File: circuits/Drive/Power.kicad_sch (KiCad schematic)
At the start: 81 parts, among them IC1 DCDC_MPM3620A, J10 Conn_01x02_Male, J11 Conn_01x02_Male, J12 Conn_01x02_Male, J13 Conn_01x02_Male, J6 USB_C_Receptacle_USB2.0, J9 Conn_01x02_Male, Q16 SSM6J808R, Q17 SSM6J808R, Q18 SSM3J332R, Q19 S8550, Q2 BSS138, Q20 SSM3J332R, Q21 S8550, Q23 S8550, Q24 SSM3J332R, Q25 S8550, Q3 SSM3J332R, Q4 BSS138, SW1 SW_SPDT_White

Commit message: ラズパイ基板とか
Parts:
- R19, R20, R65: value 2k -> 1k
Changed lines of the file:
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@@
       (effects (font (size 1.27 1.27)))
     )
-    (property "Value" "2k" (at 335.28 210.82 90)
+    (property "Value" "1k" (at 335.28 210.82 90)
       (effects (font (size 1.27 1.27)))
     )
@@
       (effects (font (size 1.27 1.27)))
     )
-    (property "Value" "2k" (at 335.28 198.12 90)
+    (property "Value" "1k" (at 335.28 198.12 90)
       (effects (font (size 1.27 1.27)))
     )
@@
       (effects (font (size 1.27 1.27)))
     )
-    (property "Value" "2k" (at 335.28 223.52 90)
+    (property "Value" "1k" (at 335.28 223.52 90)
       (effects (font (size 1.27 1.27)))
     )

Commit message: PDFプロット
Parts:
- added U1: AZ1084CD-3.3, Package_TO_SOT_SMD:TO-252-2, symbol Regulator_Linear:AMS1117CD-3.3
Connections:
- net +3.3V: now also U1.2 (VO)
- net +5V: now also U1.3 (VI)
- net GND: now also U1.1 (GND)
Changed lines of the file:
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@@
+    )
+  )
+  (symbol (lib_id "Regulator_Linear:AMS1117CD-3.3") (at 236.22 213.36 0) (unit 1)
+    (in_bom yes) (on_board yes) (dnp no) (fields_autoplaced)
+    (property "Reference" "U1" (at 236.22 207.01 0)
+      (effects (font (size 1.27 1.27)))
+    )
+    (property "Value" "AZ1084CD-3.3" (at 236.22 209.55 0)
+      (effects (font (size 1.27 1.27)))
+    )
+    (property "Footprint" "Package_TO_SOT_SMD:TO-252-2" (at 236.22 208.28 0)
+      (effects (font (size 1.27 1.27)) hide)
+    )
+    (property "Datasheet" "http://www.advanced-monolithic.com/pdf/ds1117.pdf" (at 238.76 219.71 0)
+      (effects (font (size 1.27 1.27)) hide)
+    )
+    (pin "1")
+    (pin "2")
+    (pin "3")
+    (instances
+      (project "Drive"
+        (path "/bf4fa0f7-7e40-4646-9c11-e04533c904d6/78bba271-6f80-468f-a85b-9d4b16f8bee8"
+          (reference "U1") (unit 1)
+        )
+      )
     )
   )

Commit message: panelフットプリント配置
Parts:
- U1: value AZ1084CD-3.3 -> AZ1117CH-3.3; footprint Package_TO_SOT_SMD:TO-252-2 -> Package_TO_SOT_SMD:SOT-223-3_TabPin2
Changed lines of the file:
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@@
-    )
-  )
-  (symbol (lib_id "Regulator_Linear:AMS1117CD-3.3") (at 236.22 213.36 0) (unit 1)
-    (in_bom yes) (on_board yes) (dnp no) (fields_autoplaced)
-    (property "Reference" "U1" (at 236.22 207.01 0)
-      (effects (font (size 1.27 1.27)))
-    )
-    (property "Value" "AZ1084CD-3.3" (at 236.22 209.55 0)
-      (effects (font (size 1.27 1.27)))
-    )
-    (property "Footprint" "Package_TO_SOT_SMD:TO-252-2" (at 236.22 208.28 0)
-      (effects (font (size 1.27 1.27)) hide)
-    )
-    (property "Datasheet" "http://www.advanced-monolithic.com/pdf/ds1117.pdf" (at 238.76 219.71 0)
-      (effects (font (size 1.27 1.27)) hide)
-    )
-    (pin "1")
-    (pin "2")
-    (pin "3")
-    (instances
-      (project "Drive"
-        (path "/bf4fa0f7-7e40-4646-9c11-e04533c904d6/78bba271-6f80-468f-a85b-9d4b16f8bee8"
-          (reference "U1") (unit 1)
-        )
-      )
     )
   )
@@
         )
       )
+    )
+  )
+  (symbol (lib_id "Regulator_Linear:AMS1117CD-3.3") (at 236.22 213.36 0) (unit 1)
+    (in_bom yes) (on_board yes) (dnp no) (fields_autoplaced)
+    (property "Reference" "U1" (at 236.22 207.01 0)
+      (effects (font (size 1.27 1.27)))
+    )
+    (property "Value" "AZ1117CH-3.3" (at 236.22 209.55 0)
+      (effects (font (size 1.27 1.27)))
+    )
+    (property "Footprint" "Package_TO_SOT_SMD:SOT-223-3_TabPin2" (at 236.22 208.28 0)
+      (effects (font (size 1.27 1.27)) hide)
+    )
+    (property "Datasheet" "http://www.advanced-monolithic.com/pdf/ds1117.pdf" (at 238.76 219.71 0)
+      (effects (font (size 1.27 1.27)) hide)
+    )
+    (pin "1")
+    (pin "2")
+    (pin "3")
+    (instances
+      (project "Drive"
+        (path "/bf4fa0f7-7e40-4646-9c11-e04533c904d6/78bba271-6f80-468f-a85b-9d4b16f8bee8"
+          (reference "U1") (unit 1)
+        )
+      )

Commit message: シンボル・フットプリントMyLib->TomoshibiLib置き換え
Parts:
- IC1: footprint MyLibrary:DCDC_MPM3620A -> TomoshibiLibrary:DCDC_MPM3620A; symbol MyLibrary:DCDC_MPM3620A -> TomoshibiLibrary:DCDC_MPM3620A
- L1: footprint MyLibrary:Inductor_CDPH4D19F -> TomoshibiLibrary:Inductor_CDPH4D19F
- Q16, Q17: footprint MyLibrary:Package_TSOP6F -> TomoshibiLibrary:Package_TSOP6F
- SW1: footprint MyLibrary:SW_Slide_SPDT_White -> TomoshibiLibrary:SW_Slide_SPDT_White
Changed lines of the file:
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@@
       (effects (font (size 1.27 1.27)))
     )
-    (property "Footprint" "MyLibrary:Inductor_CDPH4D19F" (at 246.38 71.12 0)
+    (property "Footprint" "TomoshibiLibrary:Inductor_CDPH4D19F" (at 246.38 71.12 0)
       (effects (font (size 1.27 1.27)) hide)
     )
@@
     )
   )
-  (symbol (lib_id "MyLibrary:DCDC_MPM3620A") (at 119.38 137.16 0) (unit 1)
+  (symbol (lib_id "TomoshibiLibrary:DCDC_MPM3620A") (at 119.38 137.16 0) (unit 1)
     (in_bom yes) (on_board yes) (dnp no)
     (property "Reference" "IC1" (at 134.62 133.35 0)
@@
       (effects (font (size 1.27 1.27)))
     )
-    (property "Footprint" "MyLibrary:DCDC_MPM3620A" (at 148.59 232.08 0)
+    (property "Footprint" "TomoshibiLibrary:DCDC_MPM3620A" (at 104.14 100.66 0)
       (effects (font (size 1.27 1.27)) (justify left top) hide)
     )
-    (property "Datasheet" "http://www.monolithicpower.com/DesktopModules/DocumentManage/API/Document/getDocument?id=3961" (at 148.59 332.08 0)
+    (property "Datasheet" "http://www.monolithicpower.com/DesktopModules/DocumentManage/API/Document/getDocument?id=3961" (at 104.14 200.66 0)
       (effects (font (size 1.27 1.27)) (justify left top) hide)
     )
@@
       (effects (font (size 1.27 1.27)))
     )
-    (property "Footprint" "MyLibrary:SW_Slide_SPDT_White" (at 203.2 40.64 0)
+    (property "Footprint" "TomoshibiLibrary:SW_Slide_SPDT_White" (at 203.2 40.64 0)
       (effects (font (size 1.27 1.27)) hide)
     )
@@
       (effects (font (size 1.27 1.27)))
     )
-    (property "Footprint" "MyLibrary:Package_TSOP6F" (at 213.36 68.58 0)
+    (property "Footprint" "TomoshibiLibrary:Package_TSOP6F" (at 213.36 68.58 0)
       (effects (font (size 1.27 1.27)) (justify left) hide)
     )
@@
       (effects (font (size 1.27 1.27)))
     )
-    (property "Footprint" "MyLibrary:Package_TSOP6F" (at 187.96 68.58 0)
+    (property "Footprint" "TomoshibiLibrary:Package_TSOP6F" (at 187.96 68.58 0)
       (effects (font (size 1.27 1.27)) (justify left) hide)
     )

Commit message: 更新
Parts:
- removed C25, C26, C39: 470uF, symbol Device:C_Polarized
- removed IC1: DCDC_MPM3620A, TomoshibiLibrary:DCDC_MPM3620A, symbol TomoshibiLibrary:DCDC_MPM3620A
- removed J10, J11, J12, J13, J9: Conn_01x02_Male, Connector_Molex:Molex_SPOX_5267-02A_1x02_P2.50mm_Vertical, symbol Connector:Conn_01x02_Male
- removed J6: USB_C_Receptacle_USB2.0, Connector_USB:USB_C_Receptacle_G-Switch_GT-USB-7010ASV, symbol Connector:USB_C_Receptacle_USB2.0
- removed Q2, Q4: BSS138, Package_TO_SOT_SMD:SOT-23, symbol Device:Q_NMOS_GSD
- removed R3: 200k, Resistor_SMD:R_0402_1005Metric, symbol Device:R
- added C11: 1uF, Capacitor_SMD:C_0402_1005Metric, symbol Device:C
- added C25, C26, C41: 22uF, Capacitor_SMD:C_0805_2012Metric, symbol Device:C
- added H1, H2: MountingHole_Pad, MountingHole:MountingHole_3.2mm_M3_Pad_Via, symbol Mechanical:MountingHole_Pad
- added J11, J2, J3, J4, J5: Conn_01x02_Pin, Connector_Molex:Molex_SPOX_5268-02A_1x02_P2.50mm_Horizontal, symbol Connector:Conn_01x02_Pin
- added J7: USB_C_Receptacle_PowerOnly_6P, Connector_USB:USB_C_Receptacle_GCT_USB4125-xx-x_6P_TopMnt_Horizontal, symbol Connector:USB_C_Receptacle_PowerOnly_6P
- added Q5, Q8: 2N7002, Package_TO_SOT_SMD:SOT-23, symbol Transistor_FET:2N7002
- added U2: DCDC_TPSM336x5, TomoshibiLibrary:DCDC_TPSM336x5, symbol TomoshibiLibrary:DCDC_TPSM336x5
- C23, C37, C38, C6: value 470uF -> 47uF; footprint (none) -> Capacitor_SMD:CP_Elec_6.3x5.4
- C32, C33: value 470uF -> 100uF; footprint (none) -> TomoshibiLibrary:Capacitor_Alum_Radial_5.0x11.0mm_Horizontal
- L1: value 22uH -> 1uH; footprint TomoshibiLibrary:Inductor_CDPH4D19F -> Inductor_SMD:L_0603_1608Metric
- R4: value 100k -> 10k
- R5: value 12k -> 20k
- R6: value 2.2k -> 5.1k
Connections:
- net +3.3V: now also C26.1
- net +5V: now also C25.1
- net +BATT: now also H1.1, J11.2 (Pin_2), J2.2 (Pin_2), J3.2 (Pin_2), J4.2 (Pin_2), J5.2 (Pin_2); no longer C38.1
- net GND: now also C11.2, C25.2, C26.2, C41.2, H2.1, J11.1 (Pin_1), J2.1 (Pin_1), J3.1 (Pin_1), J4.1 (Pin_1), J5.1 (Pin_1), J7.A12 (GND), J7.B12 (GND), J7.S1 (SHIELD), Q5.2 (S), Q8.2 (S), U2.10 (GND)
- net PG: now also R4.2, Q5.1 (G), U2.1 (PGOOD); no longer R4.1
- net PowerSW: now also Q8.1 (G)
- net VBUS: now also J7.A9 (VBUS), J7.B9 (VBUS)
- net VCC: now also C38.1, U2.2 (EN), U2.3 (VIN)
- net Vout: now also C41.1, U2.4 (VOUT)
- net at Q3.1 (G), R8.2: now also Q5.3 (D)
- net at R5.1, R6.2: now also U2.9 (FB)
- net at R64.2: now also J7.B5 (CC2)
- net at R12.2: now also Q8.3 (D)
- net at R65.2: now also J7.A5 (CC1)
- net at R1.1: now also SW1.3 (C); no longer SW1.1 (A)
- new net: C11.1, R4.1, U2.11 (RT), U2.8 (VCC)
- no-connect marks 11 -> 4
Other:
- note removed: "三端子を新しく選定したのにする 電源直付けのための穴を設定する 電源平滑コンデンサは基板設計の時に良い感じに数調整"
- note removed: "電源スイッチ 耐圧大丈夫？"
- moved on the sheet: C1, C2, C38, C40, C6, D1, Q3, R10, R4, R5, R6, R64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

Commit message: raspi基板回路図
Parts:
- SW1: footprint TomoshibiLibrary:SW_Slide_SPDT_White -> TomoshibiLibrary:SW_Slide_SPDT_IS-1235-G
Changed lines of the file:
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@@
       (effects (font (size 1.27 1.27)))
     )
-    (property "Footprint" "TomoshibiLibrary:SW_Slide_SPDT_White" (at 203.2 40.64 0)
+    (property "Footprint" "TomoshibiLibrary:SW_Slide_SPDT_IS-1235-G" (at 203.2 40.64 0)
       (effects (font (size 1.27 1.27)) hide)
     )

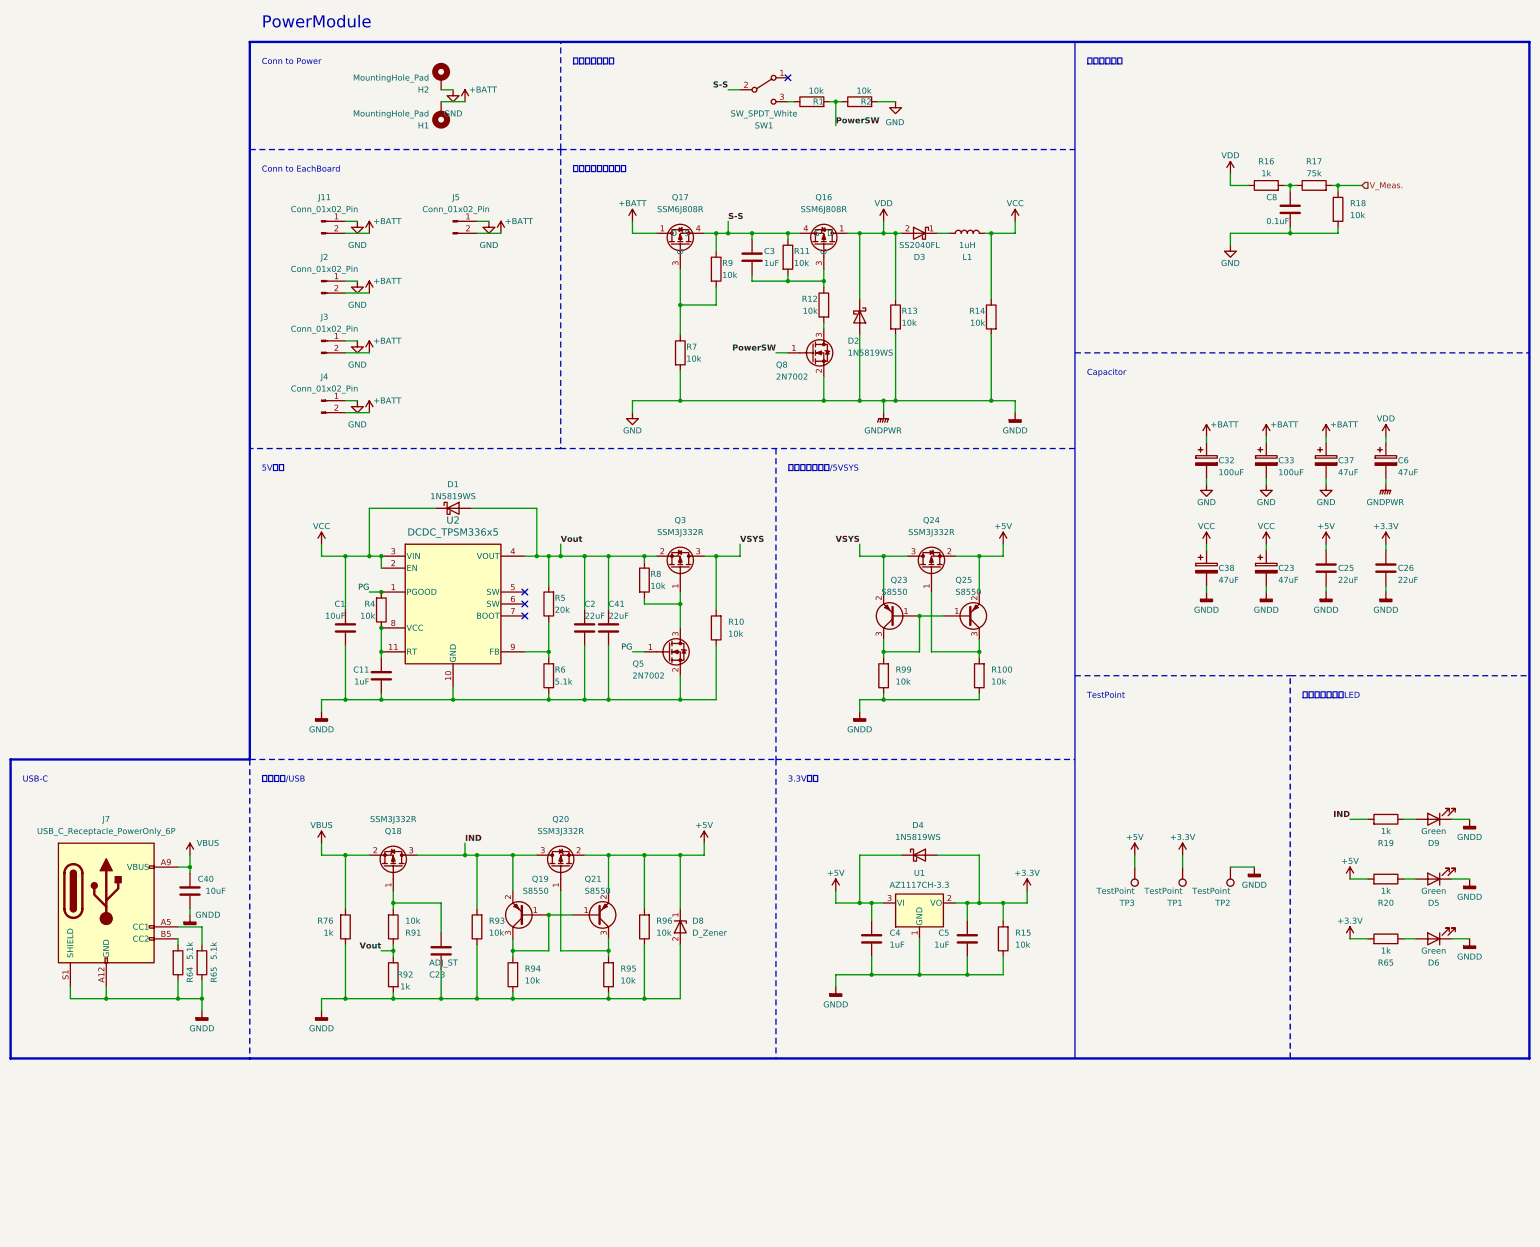
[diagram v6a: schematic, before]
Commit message: 発注_第一弾
Drive, 1stLayer_Power, 2ndLayer_3rdLayer
を発注
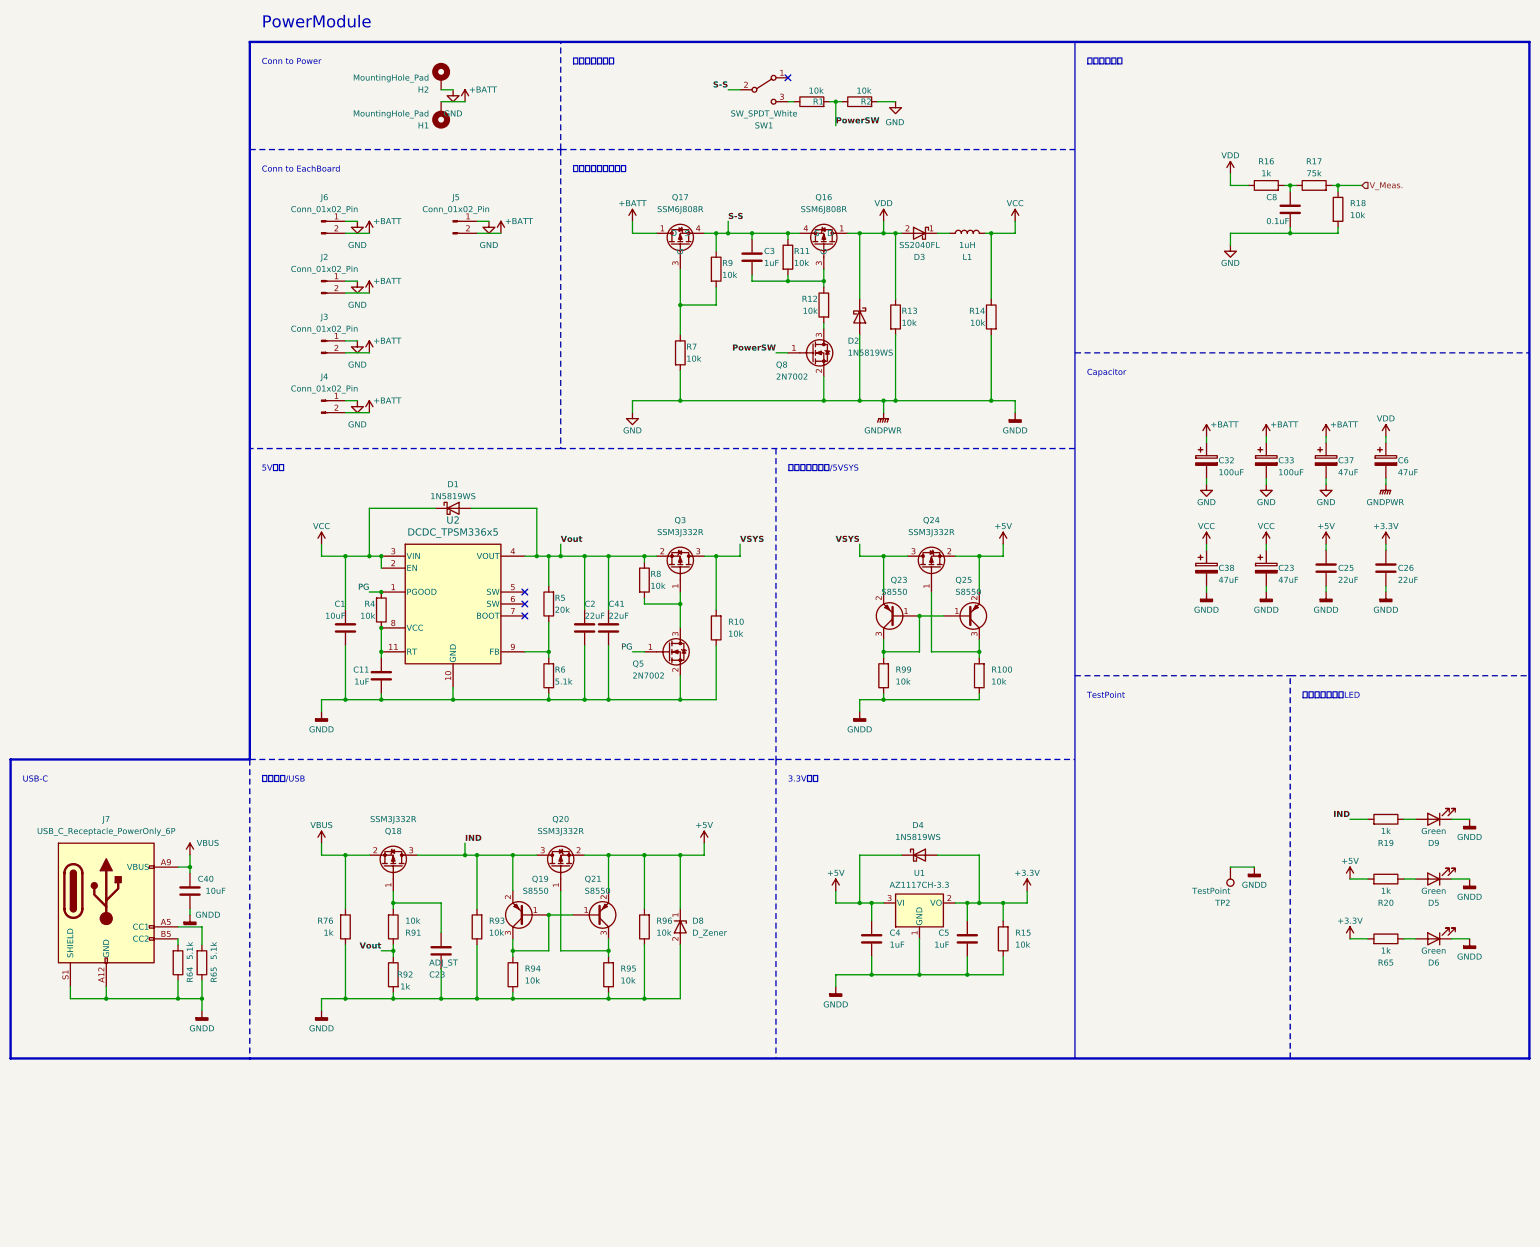
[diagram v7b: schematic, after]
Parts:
- removed TP1, TP3: TestPoint, TestPoint:TestPoint_THTPad_D2.0mm_Drill1.0mm, symbol Connector:TestPoint
- renumbered J11 to J6
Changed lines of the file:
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@@
     (stroke (width 0) (type default))
   )
-  (wire (pts (xy 292.1 203.2) (xy 292.1 205.74))
-    (stroke (width 0) (type default))
-  )
   (polyline (pts (xy 93.98 30.48) (xy 365.76 30.48))
     (stroke (width 0.5) (type solid))
@@
     (stroke (width 0) (type default))
   )
-  (wire (pts (xy 281.94 203.2) (xy 281.94 205.74))
-    (stroke (width 0) (type default))
-  )
   (wire (pts (xy 109.22 170.18) (xy 109.22 172.72))
     (stroke (width 0) (type default))
@@
     )
   )
-  (symbol (lib_id "Connector:TestPoint") (at 292.1 205.74 180) (unit 1)
-    (in_bom yes) (on_board yes) (dnp no)
-    (property "Reference" "TP1" (at 292.1 213.36 0)
-      (effects (font (size 1.27 1.27)) (justify left))
-    )
-    (property "Value" "TestPoint" (at 292.1 210.82 0)
-      (effects (font (size 1.27 1.27)) (justify left))
-    )
-    (property "Footprint" "TestPoint:TestPoint_THTPad_D2.0mm_Drill1.0mm" (at 287.02 205.74 0)
-      (effects (font (size 1.27 1.27)) hide)
-    )
-    (property "Datasheet" "~" (at 287.02 205.74 0)
-      (effects (font (size 1.27 1.27)) hide)
-    )
-    (pin "1")
-    (instances
-      (project "Main"
-        (path "/aa9d7141-7530-418f-853d-a56ee68433fb/a9430107-cf2a-4437-9d5a-ed3d69145a18"
-          (reference "TP1") (unit 1)
-        )
-      )
-      (project "Drive"
-        (path "/bf4fa0f7-7e40-4646-9c11-e04533c904d6/78bba271-6f80-468f-a85b-9d4b16f8bee8"
-          (reference "TP2") (unit 1)
-        )
-      )
-    )
-  )
   (symbol (lib_id "Device:C") (at 121.92 165.1 0) (mirror y) (unit 1)
     (in_bom yes) (on_board yes) (dnp no)
@@
     )
   )
-  (symbol (lib_id "power:+5V") (at 281.94 203.2 0) (unit 1)
-    (in_bom yes) (on_board yes) (dnp no) (fields_autoplaced)
-    (property "Reference" "#PWR06" (at 281.94 207.01 0)
-      (effects (font (size 1.27 1.27)) hide)
-    )
-    (property "Value" "+5V" (at 281.94 199.39 0)
-      (effects (font (size 1.27 1.27)))
-    )
-    (property "Footprint" "" (at 281.94 203.2 0)
-      (effects (font (size 1.27 1.27)) hide)
-    )
-    (property "Datasheet" "" (at 281.94 203.2 0)
-      (effects (font (size 1.27 1.27)) hide)
-    )
-    (pin "1")
-    (instances
-      (project "Main"
-        (path "/aa9d7141-7530-418f-853d-a56ee68433fb/a9430107-cf2a-4437-9d5a-ed3d69145a18"
-          (reference "#PWR06") (unit 1)
-        )
-      )
-      (project "Drive"
-        (path "/bf4fa0f7-7e40-4646-9c11-e04533c904d6/78bba271-6f80-468f-a85b-9d4b16f8bee8"
-          (reference "#PWR050") (unit 1)
-        )
-      )
-    )
-  )
   (symbol (lib_id "power:+5V") (at 327.66 208.28 0) (unit 1)
     (in_bom yes) (on_board yes) (dnp no) (fields_autoplaced)
@@
   (symbol (lib_id "Connector:Conn_01x02_Pin") (at 109.22 68.58 0) (unit 1)
     (in_bom yes) (on_board yes) (dnp no) (fields_autoplaced)
-    (property "Reference" "J11" (at 109.855 63.5 0)
+    (property "Reference" "J6" (at 109.855 63.5 0)
       (effects (font (size 1.27 1.27)))
     )
@@
       (project "Drive"
         (path "/bf4fa0f7-7e40-4646-9c11-e04533c904d6/78bba271-6f80-468f-a85b-9d4b16f8bee8"
-          (reference "J11") (unit 1)
+          (reference "J6") (unit 1)
         )
       )
@@
     )
   )
-  (symbol (lib_id "Connector:TestPoint") (at 281.94 205.74 180) (unit 1)
-    (in_bom yes) (on_board yes) (dnp no)
-    (property "Reference" "TP3" (at 281.94 213.36 0)
-      (effects (font (size 1.27 1.27)) (justify left))
-    )
-    (property "Value" "TestPoint" (at 281.94 210.82 0)
-      (effects (font (size 1.27 1.27)) (justify left))
-    )
-    (property "Footprint" "TestPoint:TestPoint_THTPad_D2.0mm_Drill1.0mm" (at 276.86 205.74 0)
-      (effects (font (size 1.27 1.27)) hide)
-    )
-    (property "Datasheet" "~" (at 276.86 205.74 0)
-      (effects (font (size 1.27 1.27)) hide)
-    )
-    (pin "1")
-    (instances
-      (project "Main"
-        (path "/aa9d7141-7530-418f-853d-a56ee68433fb/a9430107-cf2a-4437-9d5a-ed3d69145a18"
-          (reference "TP3") (unit 1)
-        )
-      )
-      (project "Drive"
-        (path "/bf4fa0f7-7e40-4646-9c11-e04533c904d6/78bba271-6f80-468f-a85b-9d4b16f8bee8"
-          (reference "TP1") (unit 1)
-        )
-      )
-    )
-  )
   (symbol (lib_id "Device:C") (at 134.62 223.52 0) (mirror x) (unit 1)
     (in_bom yes) (on_board yes) (dnp no)
@@
         )
       )
-    )
-  )
-  (symbol (lib_id "power:+3.3V") (at 292.1 203.2 0) (unit 1)
-    (in_bom yes) (on_board yes) (dnp no) (fields_autoplaced)
-    (property "Reference" "#PWR014" (at 292.1 207.01 0)
-      (effects (font (size 1.27 1.27)) hide)
-    )
-    (property "Value" "+3.3V" (at 292.1 199.39 0)
-      (effects (font (size 1.27 1.27)))
-    )
-    (property "Footprint" "" (at 292.1 203.2 0)
-      (effects (font (size 1.27 1.27)) hide)
-    )
-    (property "Datasheet" "" (at 292.1 203.2 0)
-      (effects (font (size 1.27 1.27)) hide)
-    )
-    (pin "1")
-    (instances
-      (project "Main"
-        (path "/aa9d7141-7530-418f-853d-a56ee68433fb/a9430107-cf2a-4437-9d5a-ed3d69145a18"
-          (reference "#PWR014") (unit 1)
-        )
-      )
-      (project "Drive"
-        (path "/bf4fa0f7-7e40-4646-9c11-e04533c904d6/78bba271-6f80-468f-a85b-9d4b16f8bee8"
-          (reference "#PWR051") (unit 1)
-        )
-      )
